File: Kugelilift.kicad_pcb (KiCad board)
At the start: 2 copper layers, 43 x 43.5 mm, 7 parts, among them J1 I2C, J4 Conn_01x05, U1 WeMos_D1_mini, U2 TCRT5000, U3 ULN2003A

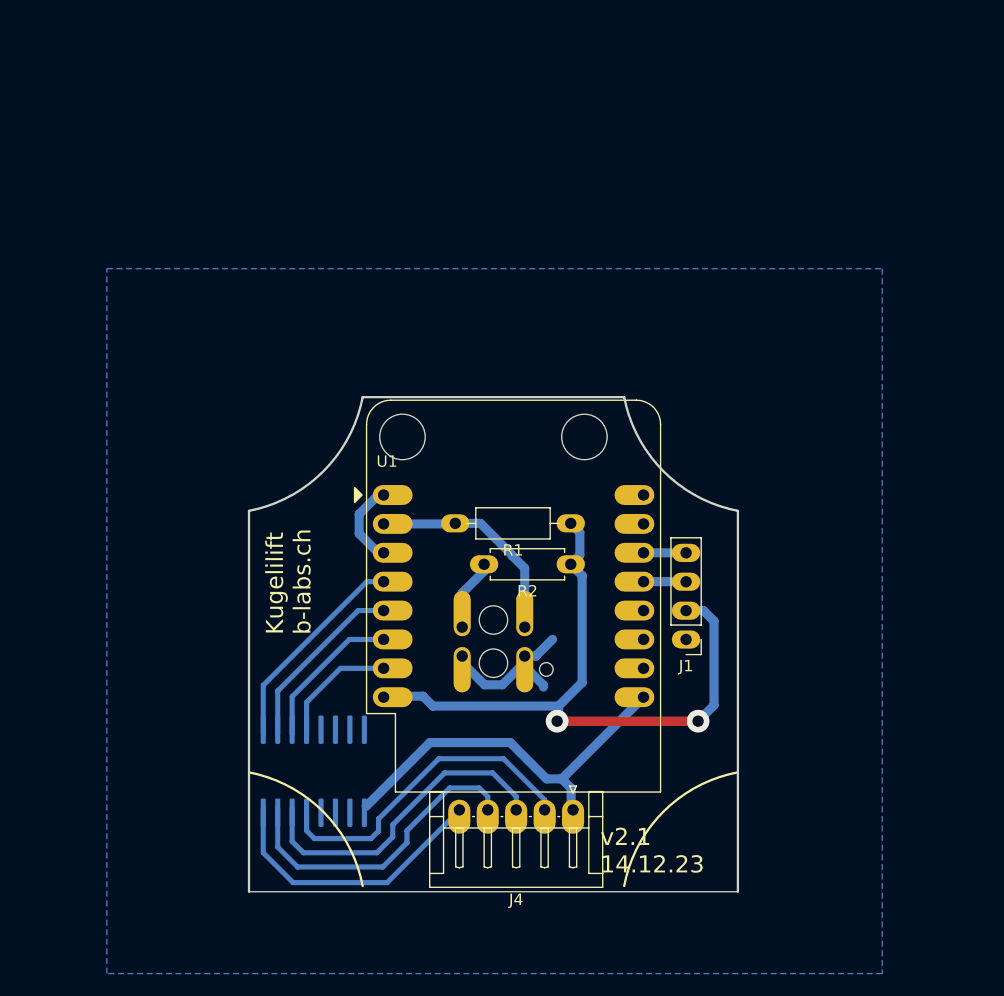
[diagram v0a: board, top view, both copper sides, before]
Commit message: Working progres with SMT ESP12 module
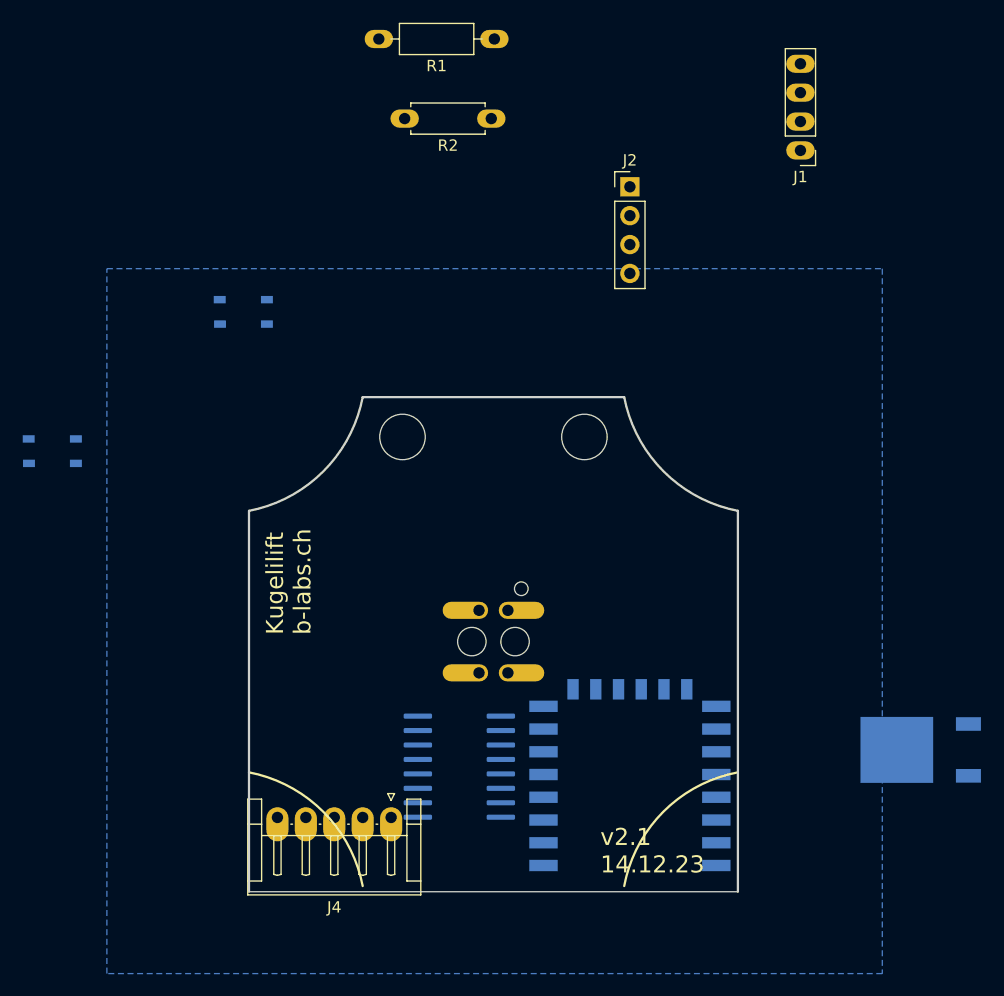
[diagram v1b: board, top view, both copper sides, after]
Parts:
- added J2: TTL, Connector_PinHeader_2.54mm:PinHeader_1x04_P2.54mm_Vertical, F.Cu at (134.0, 38.0)
- added SW1: RESET, Button_Switch_SMD:SW_Push_1P1T_NO_Vertical_Wuerth_434133025816, B.Cu at (100.0, 49.0)
- added SW2: MODE, Button_Switch_SMD:SW_Push_1P1T_NO_Vertical_Wuerth_434133025816, B.Cu at (83.2, 61.2)
- added U5: UA78M33_TO252, Package_TO_SOT_SMD:TO-252-2, B.Cu at (159.6, 87.5)
- J4: value Conn_01x05 -> Stepper
- U1: value WeMos_D1_mini -> ESP-12E; footprint Module:WEMOS_D1_mini_light -> RF_Module:ESP-12E; moved to B.Cu
- moved J1 44.2 mm to (149.0, 34.8)
- moved R1 43.1 mm to (122.1, 25.0)
- moved R2 39.8 mm to (121.8, 32.0)
- moved U1 36.3 mm to (134.0, 94.2)
- moved J4 16.0 mm to (113.0, 93.5)
- moved U3 12.8 mm to (119.0, 89.0), turned to 180 degrees
- turned U2 to -90 degrees
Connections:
- U1 pad 1: /RST -> Net-(SW1-Pad2)
- U1 pad 10: GND -> unconnected-(U1-Pad10)
- U1 pad 13: /SDA -> unconnected-(U1-Pad13)
- U1 pad 14: /SCL -> unconnected-(U1-Pad14)
- U1 pad 15: unconnected-(U1-Pad15) -> GND
- U1 pad 16: unconnected-(U1-Pad16) -> /slim-in-4
- U1 pad 3: /RST -> +3V3
- U1 pad 4: /slim-in-1 -> unconnected-(U1-Pad4)
- U1 pad 5: /slim-in-2 -> /slim-in-3
- U1 pad 6: /slim-in-3 -> /slim-in-1
- U1 pad 7: /slim-in-4 -> /slim-in-2
- U1 pad 9: +5V -> unconnected-(U1-Pad9)
- U3 pad 8: GND -> unconnected-(U3-Pad8)
- U3 pad 9: +5V -> unconnected-(U3-Pad9)
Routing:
- net +3V3: track 59.8 -> 0.00 mm, vias 2 -> 0
- net +5V: track 34.2 -> 0.00 mm
- net /slim-out-4: track 29.1 -> 0.00 mm
- net /slim-out-3: track 28.6 -> 0.00 mm
- net /slim-out-2: track 27.6 -> 0.00 mm
- net /slim-out-1: track 24.9 -> 0.00 mm
- net Net-(R1-Pad2): track 19.3 -> 0.00 mm
- net /slim-in-1: track 18.7 -> 0.00 mm
- net GND: track 16.2 -> 0.00 mm
- net /slim-in-2: track 16.1 -> 0.00 mm
- net /slim-in-3: track 13.4 -> 0.00 mm
- net /slim-in-4: track 10.8 -> 0.00 mm
- net /RST: track 7.41 -> 0.00 mm
- net Net-(R2-Pad2): track 6.33 -> 0.00 mm
- net /SDA: track 3.74 -> 0.00 mm
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
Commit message: ESP-01F based PCB
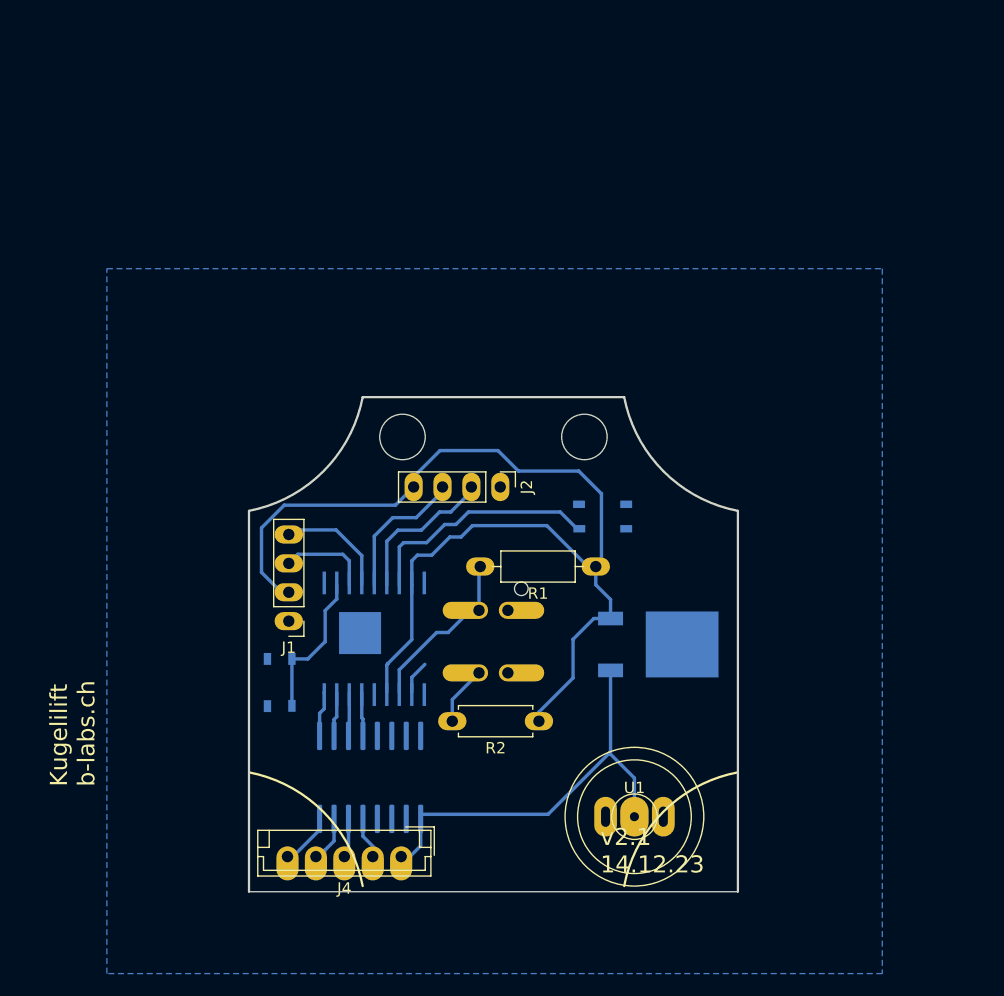
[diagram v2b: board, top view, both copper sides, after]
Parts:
- added U4: esp-01f, esp-01f:esp-01f, B.Cu at (111.5, 77.8)
- J4: footprint Connector_JST:JST_EH_S5B-EH_1x05_P2.50mm_Horizontal -> Connector_JST:JST_EH_B5B-EH-A_1x05_P2.50mm_Vertical
- U1: value ESP-12E -> magnetic-charger; footprint RF_Module:ESP-12E -> magnetic-charger:magnetic-charger; moved to F.Cu
- moved J1 61.1 mm to (104.0, 76.2)
- moved R2 53.2 mm to (126.0, 85.0)
- moved R1 47.2 mm to (131.0, 71.4)
- moved SW1 36.4 mm to (131.6, 67.0)
- moved J2 28.8 mm to (122.6, 64.4), turned to -90 degrees
- moved SW2 28.5 mm to (103.2, 81.6), turned to -90 degrees
- moved U5 24.9 mm to (136.5, 78.2), turned to 0 degrees
- moved U3 7.90 mm to (111.2, 89.9), turned to -90 degrees
- moved J4 3.55 mm to (113.9, 96.9)
- moved U1 0.89 mm to (134.4, 93.4)
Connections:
- U1 pad 1: Net-(SW1-Pad2) -> GND
- U1 pad 2: Net-(R1-Pad2) -> +5V
- U3 pad 1: /slim-in-1 -> Net-(U3-Pad1)
- U3 pad 2: /slim-in-2 -> /in-2
- U3 pad 3: /slim-in-3 -> /in-1
- U3 pad 4: /slim-in-4 -> /in-3
- U3 pad 5: /slim-in-5 -> unconnected-(U3-Pad5)
- U3 pad 8: unconnected-(U3-Pad8) -> GND
- U3 pad 9: unconnected-(U3-Pad9) -> +5V
- U5 pad 2: GND -> unconnected-(U5-Pad2)
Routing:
- net +3V3: track 0.00 -> 97.5 mm
- net +5V: track 0.00 -> 36.8 mm
- net Net-(SW1-Pad2): track 0.00 -> 21.1 mm
- net Net-(R1-Pad2): track 0.00 -> 15.1 mm
- net TX: track 0.00 -> 13.5 mm
- net Net-(SW2-Pad2): track 0.00 -> 13.1 mm
- net RX: track 0.00 -> 12.3 mm
- net /SCL: track 0.00 -> 10.1 mm
- net /SDA: track 0.00 -> 8.04 mm
- net Net-(R2-Pad2): track 0.00 -> 5.22 mm
- net /slim-out-1: track 0.00 -> 4.57 mm
- net Net-(U3-Pad1): track 0.00 -> 4.40 mm
- net /slim-out-4: track 0.00 -> 4.39 mm
- net /in-2: track 0.00 -> 4.33 mm
- net /in-3: track 0.00 -> 4.27 mm
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
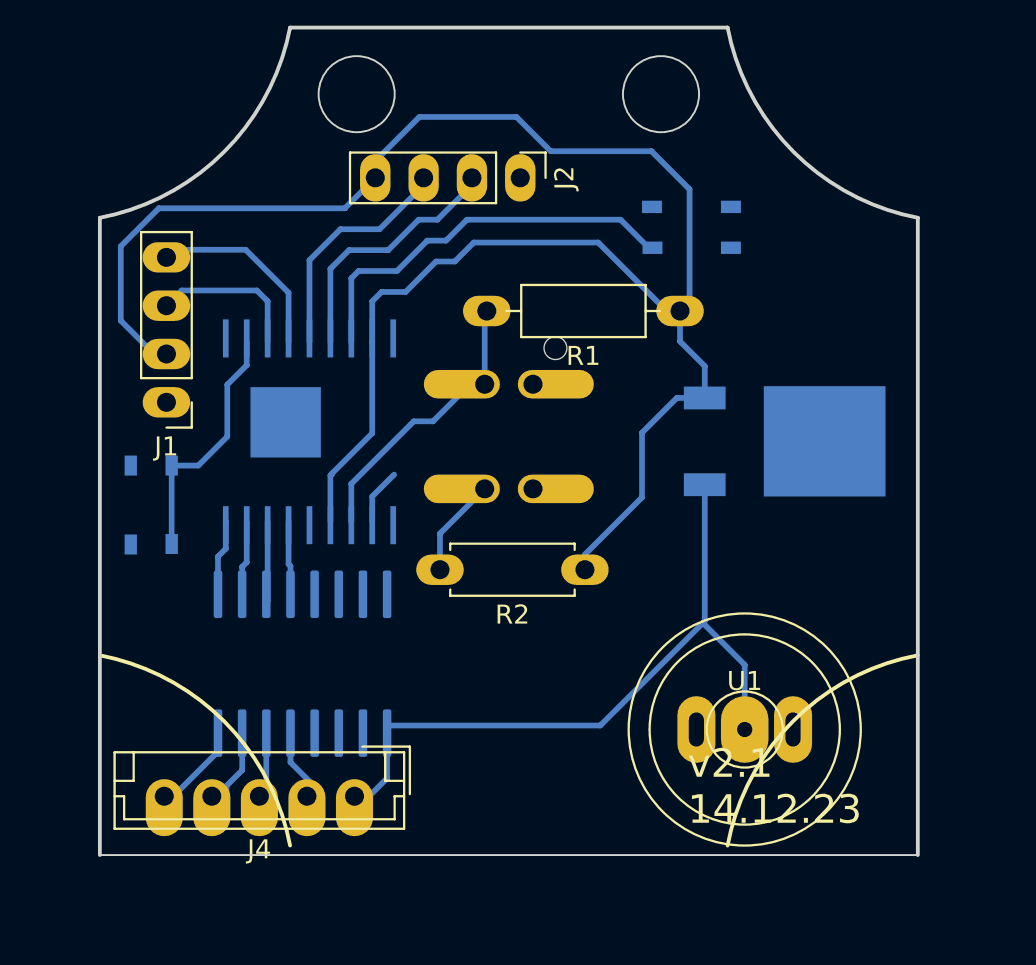
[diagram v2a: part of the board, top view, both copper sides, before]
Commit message: PCB Version 2.2
- ESP-12F
- Linear regulator + Capacitors
- ULN2003 in small SOP-16 package
- TTL instead of USB
- TCRT5000
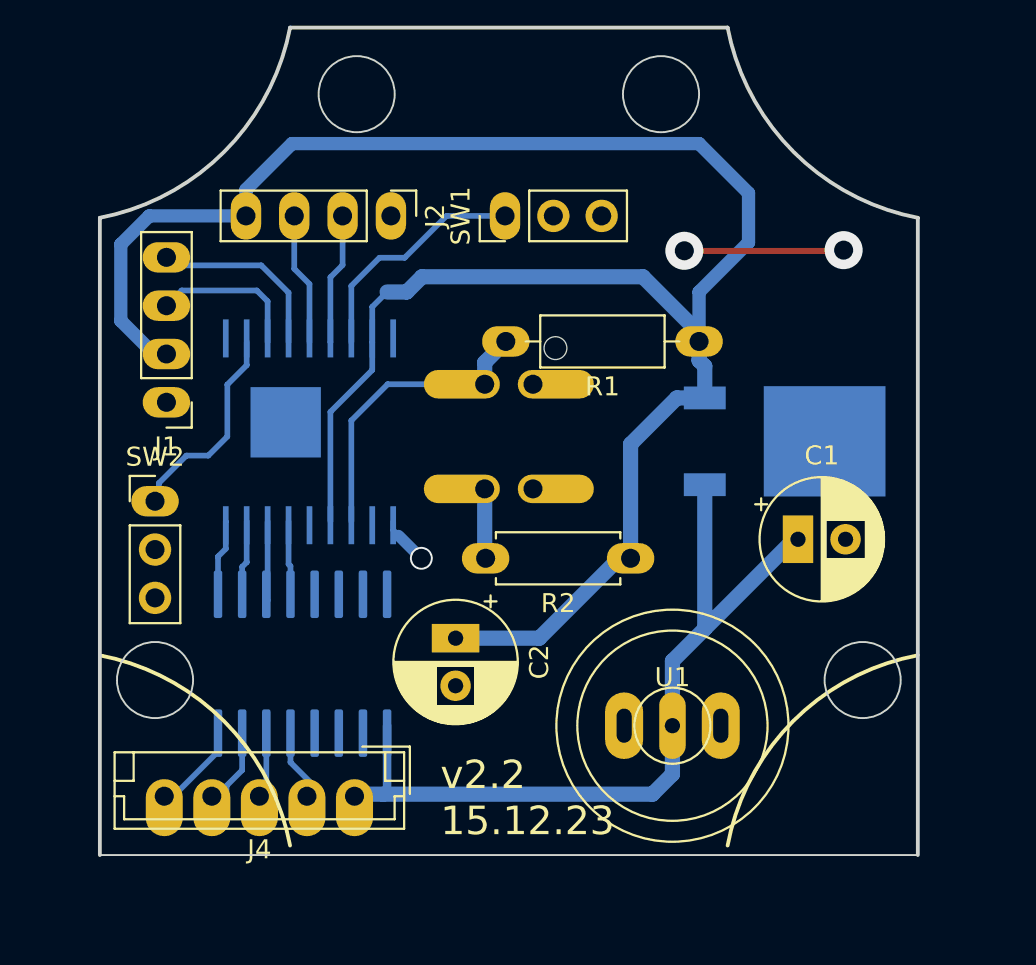
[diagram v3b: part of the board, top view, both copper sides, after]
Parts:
- added C1: C_Polarized, Capacitor_THT:CP_Radial_D6.3mm_P2.50mm, F.Cu at (137.2, 83.4)
- added C2: C_Polarized, Capacitor_THT:CP_Radial_D6.3mm_P2.50mm, F.Cu at (119.2, 88.6)
- SW1, SW2: footprint Button_Switch_SMD:SW_Push_1P1T_NO_Vertical_Wuerth_434133025816 -> Connector_PinHeader_2.54mm:PinHeader_1x03_P2.54mm_Vertical; moved to F.Cu
- moved SW1 9.82 mm to (121.8, 66.4), turned to 90 degrees
- moved J2 7.09 mm to (115.8, 66.4)
- moved U1 3.81 mm to (130.6, 93.2)
- moved R2 2.47 mm to (128.4, 84.4)
- moved R1 1.89 mm to (132.0, 73.0)
- moved SW2 0.28 mm to (103.4, 81.4), turned to 0 degrees
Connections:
- SW1 pad 1: GND -> Net-(SW1-Pad1)
- SW1 pad 2: Net-(SW1-Pad2) -> GND
- SW2 pad 1: GND -> Net-(SW2-Pad1)
- SW2 pad 2: Net-(SW2-Pad2) -> GND
- U4 pad 11: Net-(SW2-Pad2) -> Net-(SW2-Pad1)
- U4 pad 16: Net-(SW1-Pad2) -> Net-(SW1-Pad1)
- U5 pad 2: unconnected-(U5-Pad2) -> GND
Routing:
- net Net-(SW1-Pad2): track 21.1 -> 0.00 mm
- net Net-(SW2-Pad2): track 13.1 -> 0.00 mm
- net Net-(SW1-Pad1): track 0.00 -> 12.6 mm
- net +3V3: track 97.5 -> 109.7 mm
- net Net-(SW2-Pad1): track 0.00 -> 10.1 mm
- net +5V: track 36.8 -> 43.8 mm
- net TX: track 13.5 -> 6.91 mm
- net GND: track 2.94 -> 8.59 mm, vias 0 -> 2
- net RX: track 12.3 -> 6.97 mm
- net unconnected-(U4-Pad1): track 0.00 -> 2.55 mm, vias 0 -> 1
- net Net-(R2-Pad2): track 5.22 -> 3.67 mm
- net Net-(R1-Pad2): track 15.1 -> 15.8 mm
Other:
- outline, holes or cut-outs redrawn
- board text added: "v2.2 15.12.23"
- board text removed: "v2.1 14.12.23"

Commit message: Prepare for milling
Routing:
- net unconnected-(U4-Pad1): track 2.55 -> 3.32 mm
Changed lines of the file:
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@@
     (fp_line (start -1.128972 -1.6885) (end -1.128972 -1.0585) (layer "F.Fab") (width 0.1))
     (fp_circle (center 1.25 0) (end 4.4 0) (layer "F.Fab") (width 0.1) (fill none))
-    (pad "1" thru_hole rect (at 0 0) (size 1.6 2.5) (drill 0.8) (layers *.Cu *.Mask)
+    (pad "1" thru_hole rect (at 0 0) (size 1.6 2.5) (drill 1) (layers *.Cu *.Mask)
       (net 3 "+5V") (pintype "passive"))
-    (pad "2" thru_hole circle (at 2.5 0) (size 1.6 1.6) (drill 0.8) (layers *.Cu *.Mask)
+    (pad "2" thru_hole circle (at 2.5 0) (size 1.6 1.6) (drill 1) (layers *.Cu *.Mask)
       (net 4 "GND") (pintype "passive"))
     (model "${KICAD6_3DMODEL_DIR}/Capacitor_THT.3dshapes/CP_Radial_D6.3mm_P2.50mm.wrl"
@@
     (fp_line (start -1.128972 -1.6885) (end -1.128972 -1.0585) (layer "F.Fab") (width 0.1))
     (fp_circle (center 1.25 0) (end 4.4 0) (layer "F.Fab") (width 0.1) (fill none))
-    (pad "1" thru_hole rect (at 0 0 270) (size 1.5 2.5) (drill 0.8) (layers *.Cu *.Mask)
+    (pad "1" thru_hole rect (at 0 0 270) (size 1.5 2.5) (drill 1) (layers *.Cu *.Mask)
       (net 2 "+3V3") (pintype "passive"))
-    (pad "2" thru_hole circle (at 2.5 0 270) (size 1.6 1.6) (drill 0.8) (layers *.Cu *.Mask)
+    (pad "2" thru_hole circle (at 2.5 0 270) (size 1.6 1.6) (drill 1) (layers *.Cu *.Mask)
       (net 4 "GND") (pintype "passive"))
     (model "${KICAD6_3DMODEL_DIR}/Capacitor_THT.3dshapes/CP_Radial_D6.3mm_P2.50mm.wrl"
@@
     (pad "1" thru_hole oval (at 2.54 0 90) (size 3.5 2) (drill oval 1.8 0.8) (layers *.Cu *.Mask)
       (net 4 "GND") (pinfunction "GND") (pintype "power_in"))
-    (pad "2" thru_hole oval (at 0 0) (size 1.4 3.5) (drill 0.8) (layers *.Cu *.Mask)
+    (pad "2" thru_hole oval (at 0 0) (size 1.4 3.5) (drill 1) (layers *.Cu *.Mask)
       (net 3 "+5V") (pinfunction "VCC") (pintype "power_in"))
     (model "${KIPRJMOD}/lib/magnetic-charger/magnetic-charger.step"
@@
   (segment (start 139.56591 68.23409) (end 139.6 68.2) (width 0.3) (layer "F.Cu") (net 4))
   (segment (start 131.22536 68.23409) (end 139.56591 68.23409) (width 0.3) (layer "F.Cu") (net 4))
-  (via (at 131.22536 68.23409) (size 2) (drill 1) (layers "F.Cu" "B.Cu") (net 4))
-  (via (at 139.6 68.2) (size 2) (drill 1) (layers "F.Cu" "B.Cu") (net 4))
+  (via (at 131.22536 68.23409) (size 2) (drill 1.1) (layers "F.Cu" "B.Cu") (net 4))
+  (via (at 139.6 68.2) (size 2) (drill 1.1) (layers "F.Cu" "B.Cu") (net 4))
   (segment (start 131.028505 68.23409) (end 131.22536 68.23409) (width 0.3) (layer "B.Cu") (net 4))
   (segment (start 106.71 93.190671) (end 106.71 94.559402) (width 0.3) (layer "B.Cu") (net 10))
@@
   (segment (start 112.619901 69.625169) (end 113.26 68.985071) (width 0.3) (layer "B.Cu") (net 25))
   (segment (start 112.619402 73.04) (end 112.619901 73.039501) (width 0.3) (layer "B.Cu") (net 25))
-  (via (at 117.4 84.4) (size 1.2) (drill 1) (layers "F.Cu" "B.Cu") (net 26))
+  (via (at 117.8 85) (size 2) (drill 1) (layers "F.Cu" "B.Cu") (net 26))
+  (segment (start 116.2 83.2) (end 117.8 84.8) (width 0.6) (layer "B.Cu") (net 26))
   (segment (start 115.919402 82.919402) (end 116.2 83.2) (width 0.3) (layer "B.Cu") (net 26))
-  (segment (start 117.4 84.4) (end 116.2 83.2) (width 0.6) (layer "B.Cu") (net 26))
+  (segment (start 117.8 84.8) (end 117.8 85) (width 0.6) (layer "B.Cu") (net 26))
   (segment (start 115.919402 82.46) (end 115.919402 82.919402) (width 0.3) (layer "B.Cu") (net 26))
   (segment (start 116.524874 68.6) (end 118.724874 66.4) (width 0.3) (layer "B.Cu") (net 28))
